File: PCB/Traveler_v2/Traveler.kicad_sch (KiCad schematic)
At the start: 36 parts, among them J1 Conn_01x06_motFL, J2 Conn_01x06_motFR, J3 Conn_01x06_motBL, J4 Conn_01x06_motBR, J5 Conn_batt, U1 ESP32-DEVKITC, U2 171013801, U4 DRV8411APWPR, U5 DRV8411APWPR

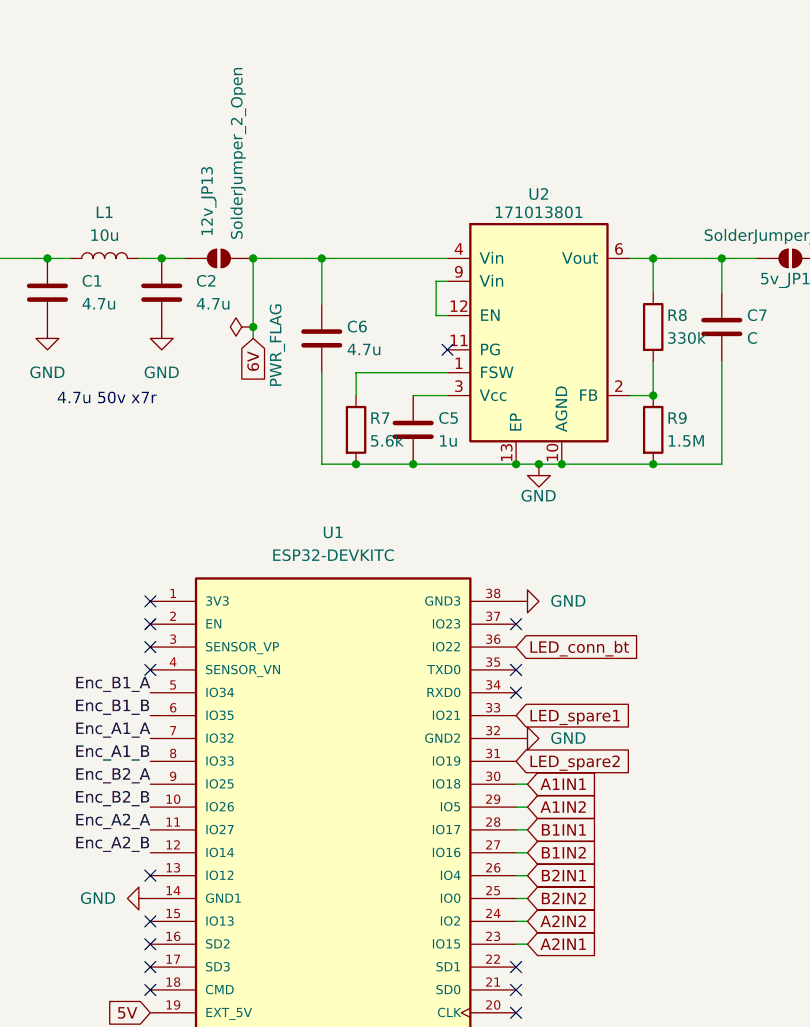
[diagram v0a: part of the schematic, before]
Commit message: Finition PCB et envoi vers fabrication
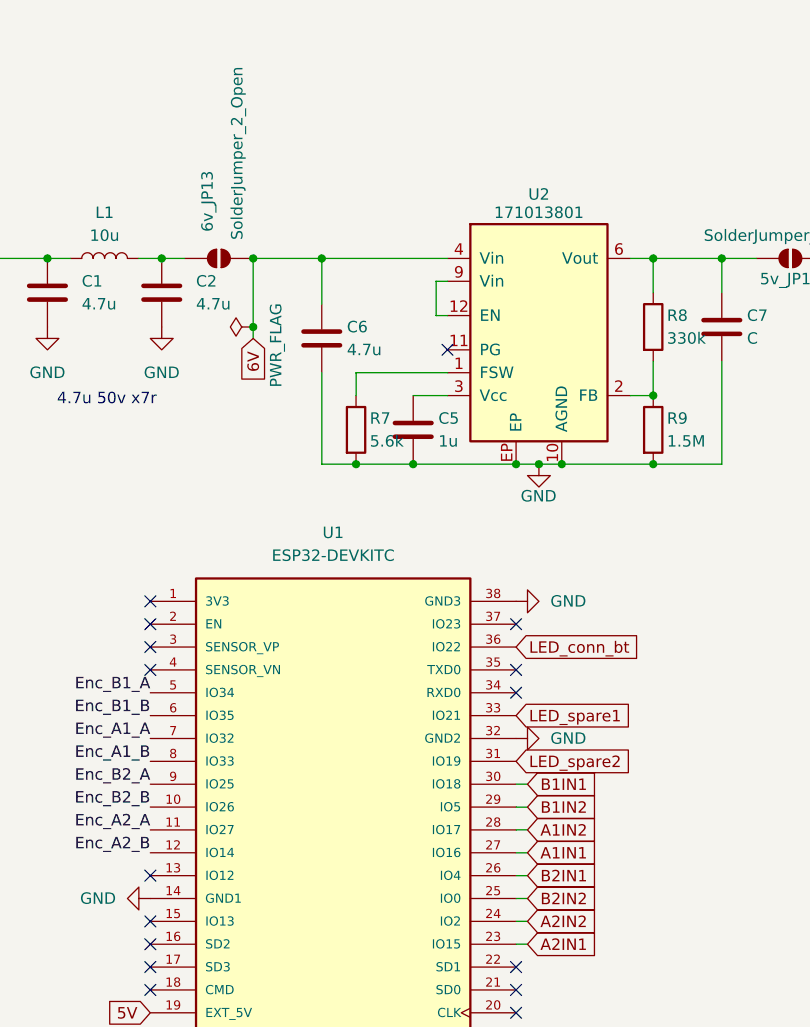
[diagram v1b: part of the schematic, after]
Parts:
- renumbered 12v_JP13 to 6v_JP13
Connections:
- net A1IN1: now also U1.27 (IO16); no longer U1.30 (IO18)
- net A1IN2: now also U1.28 (IO17); no longer U1.29 (IO5)
- net B1IN1: now also U1.30 (IO18); no longer U1.28 (IO17)
- net B1IN2: now also U1.29 (IO5); no longer U1.27 (IO16)
- net GND: now also U2.EP; no longer U2.13 (EP)
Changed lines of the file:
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@@
 	(wire
 		(pts
-			(xy 64.77 43.18) (xy 64.77 48.26)
+			(xy 87.63 104.14) (xy 86.36 104.14)
 		)
 		(stroke
@@
 	(wire
 		(pts
-			(xy 87.63 109.22) (xy 86.36 109.22)
+			(xy 64.77 43.18) (xy 64.77 48.26)
 		)
 		(stroke
@@
 	(wire
 		(pts
+			(xy 87.63 106.68) (xy 86.36 106.68)
+		)
+		(stroke
+			(width 0)
+			(type default)
+		)
+	)
+	(wire
+		(pts
 			(xy 64.77 55.88) (xy 64.77 66.04)
 		)
@@
 	(wire
 		(pts
+			(xy 87.63 101.6) (xy 86.36 101.6)
+		)
+		(stroke
+			(width 0)
+			(type default)
+		)
+	)
+	(wire
+		(pts
 			(xy 74.93 58.42) (xy 78.74 58.42)
 		)
@@
 	(wire
 		(pts
-			(xy 87.63 104.14) (xy 86.36 104.14)
-		)
-		(stroke
-			(width 0)
-			(type default)
-		)
-	)
-	(wire
-		(pts
 			(xy 248.92 39.37) (xy 257.81 39.37)
 		)
@@
 	(wire
 		(pts
-			(xy 87.63 101.6) (xy 86.36 101.6)
-		)
-		(stroke
-			(width 0)
-			(type default)
-		)
-	)
-	(wire
-		(pts
 			(xy 78.74 43.18) (xy 64.77 43.18)
 		)
@@
 	(wire
 		(pts
-			(xy 87.63 106.68) (xy 86.36 106.68)
-		)
-		(stroke
-			(width 0)
-			(type default)
-		)
-	)
-	(wire
-		(pts
 			(xy 101.6 43.18) (xy 109.22 43.18)
 		)
@@
 	(wire
 		(pts
+			(xy 87.63 109.22) (xy 86.36 109.22)
+		)
+		(stroke
+			(width 0)
+			(type default)
+		)
+	)
+	(wire
+		(pts
 			(xy 248.92 64.77) (xy 257.81 64.77)
 		)
@@
 	(global_label "A1IN2"
 		(shape input)
-		(at 87.63 104.14 0)
+		(at 87.63 106.68 0)
 		(fields_autoplaced yes)
 		(effects
@@
 		)
 		(property "Intersheetrefs" "${INTERSHEET_REFS}"
-			(at 96.0581 104.14 0)
+			(at 96.0581 106.68 0)
 			(effects
 				(font
@@
 	(global_label "A1IN1"
 		(shape input)
-		(at 87.63 101.6 0)
+		(at 87.63 109.22 0)
 		(fields_autoplaced yes)
 		(effects
@@
 		)
 		(property "Intersheetrefs" "${INTERSHEET_REFS}"
-			(at 96.0581 101.6 0)
+			(at 96.0581 109.22 0)
 			(effects
 				(font
@@
 	(global_label "B1IN1"
 		(shape input)
-		(at 87.63 106.68 0)
+		(at 87.63 101.6 0)
 		(fields_autoplaced yes)
 		(effects
@@
 		)
 		(property "Intersheetrefs" "${INTERSHEET_REFS}"
-			(at 96.2395 106.68 0)
+			(at 96.2395 101.6 0)
 			(effects
 				(font
@@
 	(global_label "B1IN2"
 		(shape input)
-		(at 87.63 109.22 0)
+		(at 87.63 104.14 0)
 		(fields_autoplaced yes)
 		(effects
@@
 		)
 		(property "Intersheetrefs" "${INTERSHEET_REFS}"
-			(at 96.2395 109.22 0)
+			(at 96.2395 104.14 0)
 			(effects
 				(font
@@
 		(pin "10"
 		)
-		(pin "13"
+		(pin "EP"
 		)
 		(pin "4"
@@
 		(on_board yes)
 		(dnp no)
-		(property "Reference" "12v_JP13"
+		(property "Reference" "6v_JP13"
 			(at 52.07 36.83 90)
 			(effects
@@
 			(project "Traveler"
 				(path "/329c0ead-d3da-412d-af02-2baef48d1278"
-					(reference "12v_JP13")
+					(reference "6v_JP13")
 					(unit 1)
 				)

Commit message: erreur avec le ldo, ordre des pins inversé sur KiCad, composant à souder en araignée
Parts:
- C7: value C -> 10u
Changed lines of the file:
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@@
 			)
 		)
-		(property "Value" "C"
+		(property "Value" "10u"
 			(at 112.014 52.07 0)
 			(effects
